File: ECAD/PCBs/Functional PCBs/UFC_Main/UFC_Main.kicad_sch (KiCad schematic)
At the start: 240 parts, among them J1 EXT_PWR, J2 ENC1, J3 VOL1, J4 BRT, J5 AP KB, J6 HUD BIT, J7 ENC2, J8 VOL2, J9 ADF SW, Q2 2N7002, Q4 ME2328-G, Q5 ME2328-G, Q6 ME2328-G, Q7 ME2328-G, Q8 ME2328-G, SW1 B3F-1026, U1 HT1621B, U10 TCA8418RTWR, U11 GN1640T, U12 GN1640T, U2 GN1640T, U3 GN1640T, U4 GN1640T, U5 GN1640T, U6 GN1640T, U7 GN1640T, U8 TXS0108EPWR, U9 TXS0108EPWR

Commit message: Updated scratchpad driver and power circuit
- Increased Board Rev to 6.2.0
- Change scratchpad driver vLCD resistor from 10k to 10ohm with a 10K trim pot in series.
  - **Justification:** Maximize the hardware-set brightness range.
- Power circuit changes:
  - **D39:** Change to [schottkey diode.](https://jlcpcb.com/partdetail/Goodwork-K24/C908664)
  - **Between Pin 2 of Q5 and VCC_SNS:** Add 10k pulldown to ground.
  - **Justification:** Did not function as intended.
    - [Link to new simulation](https://tinyurl.com/26gh26ra)

TBD:  **Q4, Q5, Q7, Q8:** Change to [p-channel MOSFETs from n-channel.](https://jlcpcb.com/partdetail/Shikues-SKML5203/C475707)
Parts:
- added R5: 10K, Resistor_SMD:R_0603_1608Metric, symbol Device:R_Small
- added RV2: 10K, Potentiometer_THT:Potentiometer_Bourns_3386P_Vertical, symbol Device:R_Potentiometer_Trim
- D39: value 1N4004W -> K24; symbol Diode:1N4004 -> Device:D_Schottky; LCSC C162732 -> C908664; Manufacturer PN 1N4001W -> K24; PN 1N4001W -> K24
- R2: value 10K -> 10; footprint Resistor_SMD:R_0603_1608Metric -> Capacitor_SMD:C_0402_1005Metric_Pad0.74x0.62mm_HandSolder; LCSC C25804 -> C25077; Manufacturer PN 0603WAF1002T5E -> 0402WGF100JTCE; PN 0603WAF1002T5E -> 0402WGF100JTCE
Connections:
- net +5V: now also RV2.1; no longer R2.1
- net GND: now also R5.2, RV2.3
- net VCC_SNS@3.3V: now also R5.1
- new net: R2.1, RV2.2
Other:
- moved on the sheet: R2

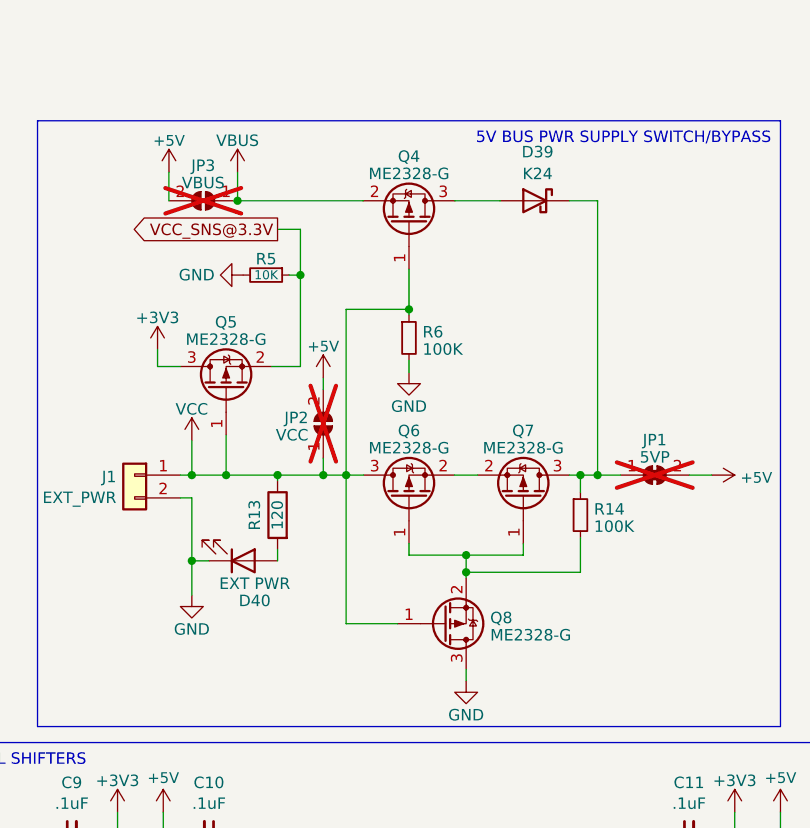
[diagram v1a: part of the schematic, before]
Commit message: Schematics (#1113)
- Q8
	changed Symbol to n-channel
      	switched drain and source
	Updated Datasheet and description
- Q4, Q6, Q7
	changed Part to SKML5203
	Updated Datasheet, description, LCSC and PN
PCB
- Q8
	Update routing according to schematic

Co-authored-by: scuba82 <christian_thalhammer@gmx.at>
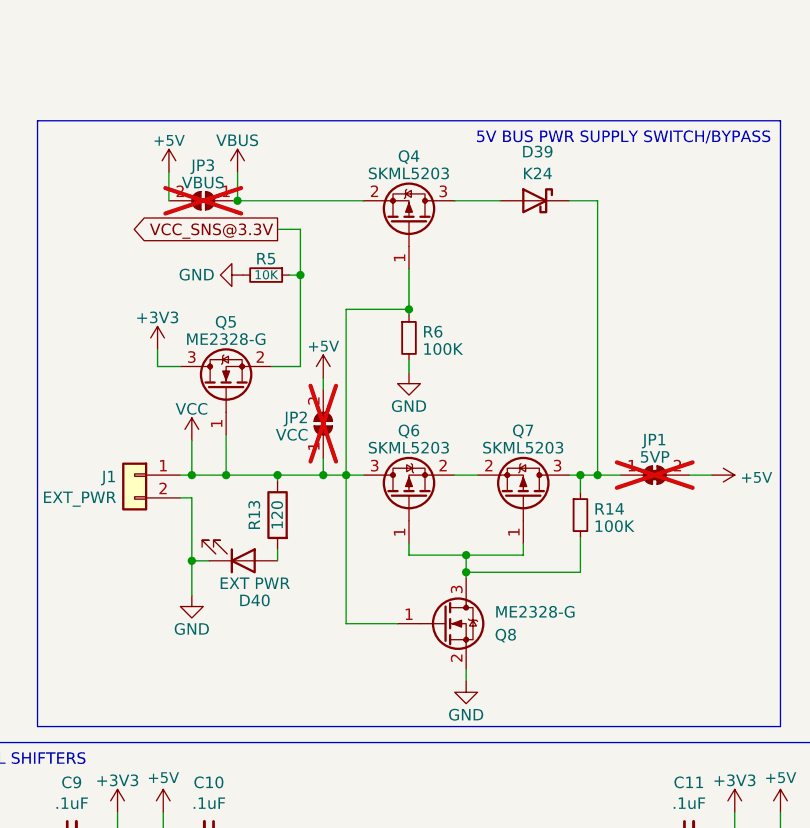
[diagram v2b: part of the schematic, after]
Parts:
- Q4, Q6, Q7: value ME2328-G -> SKML5203; LCSC C709746 -> C475707; PN ME2328-G -> SKML5203
- Q5, Q8: footprint Package_TO_SOT_SMD:SOT-23 -> Package_TO_SOT_SMD:SOT-323_SC-70; symbol Transistor_FET:BSS84 -> Transistor_FET:BSS214NW
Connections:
- net GND: now also Q8.2 (S); no longer Q8.3 (D)
- net at Q6.1 (G), Q7.1 (G), R14.2: now also Q8.3 (D); no longer Q8.2 (S)
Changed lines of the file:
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@@
 			)
 		)
-		(property "Value" "ME2328-G"
+		(property "Value" "SKML5203"
 			(at 709.295 62.4111 90)
 			(effects
@@
 			)
 		)
-		(property "Datasheet" "https://www.vishay.com/docs/68741/si2301cd.pdf"
+		(property "Datasheet" "https://www.lcsc.com/datasheet/lcsc_datasheet_2001131004_Shikues-SKML5203_C475707.pdf"
 			(at 709.295 67.945 0)
 			(effects
@@
 			)
 		)
-		(property "Description" ""
+		(property "Description" "30V 4A 65mΩ@10V,4A 1.3V@250uA 1 Piece P-Channel SOT-23 MOSFETs ROHS"
 			(at 709.295 67.945 0)
 			(effects
@@
 			)
 		)
-		(property "LCSC" "C709746"
+		(property "LCSC" "C475707"
 			(at 709.295 67.945 90)
 			(effects
@@
 			)
 		)
-		(property "PN" "ME2328-G"
+		(property "PN" "SKML5203"
 			(at 709.295 67.945 90)
 			(effects
@@
 			)
 		)
-		(property "Value" "ME2328-G"
+		(property "Value" "SKML5203"
 			(at 721.995 62.4111 90)
 			(effects
@@
 			)
 		)
-		(property "Datasheet" "https://www.vishay.com/docs/68741/si2301cd.pdf"
+		(property "Datasheet" "https://www.lcsc.com/datasheet/lcsc_datasheet_2001131004_Shikues-SKML5203_C475707.pdf"
 			(at 721.995 67.945 0)
 			(effects
@@
 			)
 		)
-		(property "Description" ""
+		(property "Description" "30V 4A 65mΩ@10V,4A 1.3V@250uA 1 Piece P-Channel SOT-23 MOSFETs ROHS"
 			(at 721.995 67.945 0)
 			(effects
@@
 			)
 		)
-		(property "LCSC" "C709746"
+		(property "LCSC" "C475707"
 			(at 721.995 67.945 90)
 			(effects
@@
 			)
 		)
-		(property "PN" "ME2328-G"
+		(property "PN" "SKML5203"
 			(at 721.995 67.945 90)
 			(effects
@@
 	)
 	(symbol
-		(lib_id "Transistor_FET:BSS84")
+		(lib_id "Transistor_FET:BSS214NW")
 		(at 713.105 81.915 0)
-		(mirror x)
 		(unit 1)
 		(exclude_from_sim no)
@@
 		(on_board yes)
 		(dnp no)
-		(fields_autoplaced yes)
 		(property "Reference" "Q8"
-			(at 718.312 81.2713 0)
+			(at 718.82 83.1851 0)
 			(effects
 				(font
@@
 		)
 		(property "Value" "ME2328-G"
-			(at 718.312 83.1923 0)
+			(at 718.82 80.6451 0)
 			(effects
 				(font
@@
 			)
 		)
-		(property "Footprint" "Package_TO_SOT_SMD:SOT-23"
-			(at 718.185 80.01 0)
+		(property "Footprint" "Package_TO_SOT_SMD:SOT-323_SC-70"
+			(at 718.185 83.82 0)
 			(effects
 				(font
@@
 			)
 		)
-		(property "Datasheet" "https://www.vishay.com/docs/68741/si2301cd.pdf"
-			(at 713.105 81.915 0)
+		(property "Datasheet" "https://www.lcsc.com/datasheet/lcsc_datasheet_2007241236_MATSUKI-ME2328-G_C709746.pdf"
+			(at 718.185 85.725 0)
 			(effects
 				(font
@@
 			)
 		)
-		(property "Description" ""
+		(property "Description" "105V 1.5A 230mΩ@10V,1.5A 1.3W 2V@250uA 1 N-Channel SOT-23 MOSFETs ROHS"
 			(at 713.105 81.915 0)
 			(effects
@@
 			)
 		)
-		(property "Value" "ME2328-G"
+		(property "Value" "SKML5203"
 			(at 709.295 31.9311 90)
 			(effects
@@
 			)
 		)
-		(property "Datasheet" "https://www.vishay.com/docs/68741/si2301cd.pdf"
+		(property "Datasheet" "https://www.lcsc.com/datasheet/lcsc_datasheet_2001131004_Shikues-SKML5203_C475707.pdf"
 			(at 709.295 37.465 0)
 			(effects
@@
 			)
 		)
-		(property "Description" ""
+		(property "Description" "30V 4A 65mΩ@10V,4A 1.3V@250uA 1 Piece P-Channel SOT-23 MOSFETs ROHS"
 			(at 709.295 37.465 0)
 			(effects
@@
 			)
 		)
-		(property "LCSC" "C709746"
+		(property "LCSC" "C475707"
 			(at 709.295 37.465 90)
 			(effects
@@
 			)
 		)
-		(property "PN" "ME2328-G"
+		(property "PN" "SKML5203"
 			(at 709.295 37.465 90)
 			(effects
@@
 	)
 	(symbol
-		(lib_id "Transistor_FET:BSS84")
+		(lib_id "Transistor_FET:BSS214NW")
 		(at 688.975 55.88 90)
 		(unit 1)
@@
 			)
 		)
-		(property "Footprint" "Package_TO_SOT_SMD:SOT-23"
+		(property "Footprint" "Package_TO_SOT_SMD:SOT-323_SC-70"
 			(at 690.88 50.8 0)
 			(effects
@@
 			)
 		)
-		(property "Datasheet" "https://www.vishay.com/docs/68741/si2301cd.pdf"
-			(at 688.975 55.88 0)
+		(property "Datasheet" "https://www.lcsc.com/datasheet/lcsc_datasheet_2007241236_MATSUKI-ME2328-G_C709746.pdf"
+			(at 692.785 50.8 0)
 			(effects
 				(font
@@
 			)
 		)
-		(property "Description" ""
+		(property "Description" "105V 1.5A 230mΩ@10V,1.5A 1.3W 2V@250uA 1 N-Channel SOT-23 MOSFETs ROHS"
 			(at 688.975 55.88 0)
 			(effects

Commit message: Added ADC for pots; changed BIT LED values
Added U13 & C18 (ADS115IDGS 4-CHANNEL ADC)
Rerouted pots to ADC from MC. (Cause ESP32 ADC sucks.)
Changed R43 & R44 from 68ohm to 120ohm to reduce brightness of BIT LEDs.
Generated fab package.
Updated files in release folder.
Was unable to reasonably move OPT 4/5 cues to new driver from COMM 2 driver. (Non-critical.)

Co-Authored-By: Oscar Arias <12484797+amanuense@users.noreply.github.com>
Co-Authored-By: Sandra Carroll <19305697+kbastronomics@users.noreply.github.com>
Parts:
- added C18: 10uF, Capacitor_SMD:C_0805_2012Metric, symbol Device:C_Small
- added U13: ADS1115IDGSR, Package_SO:VSSOP-10_3x3mm_P0.5mm, symbol Analog_ADC:ADS1115IDGS
- R43, R44: value 68 -> 120; LCSC C27592 -> C22787; Manufacturer PN 0603WAF680JT5E -> 0603WAF1200T5E; PN 0603WAF680JT5E -> 0603WAF1200T5E
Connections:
- net +3V3: now also C18.2, U13.8 (VDD)
- net GND: now also C18.1, U13.1 (ADDR), U13.3 (GND)
- net SCL@3.3V: now also U13.10 (SCL)
- net SDA@3.3V: now also U13.9 (SDA)
- net ANALOG1@3.3V renamed AIN1
- net AIN1: now also U13.5 (AIN1); no longer MC1.9 (IO1)
- net ANALOG2@3.3V renamed AIN0
- net AIN0: now also U13.4 (AIN0); no longer MC1.10 (IO2)
- net ANALOG3@3.3V renamed AIN2
- net AIN2: now also U13.6 (AIN2); no longer MC1.2 (IO3)
- new net ADC_RDY@3.3V: MC1.9 (IO1), U13.2 (ALERT/RDY)
- no-connect marks 123 -> 126
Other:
- note added: "ADDR GND: 1001000 VDD: 1001001 SDA: 1001010 SCL: 1001011"
- moved on the sheet: C5, C6, C7, C8, D69, D70, D71, D72, D73, D74, D75, D76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

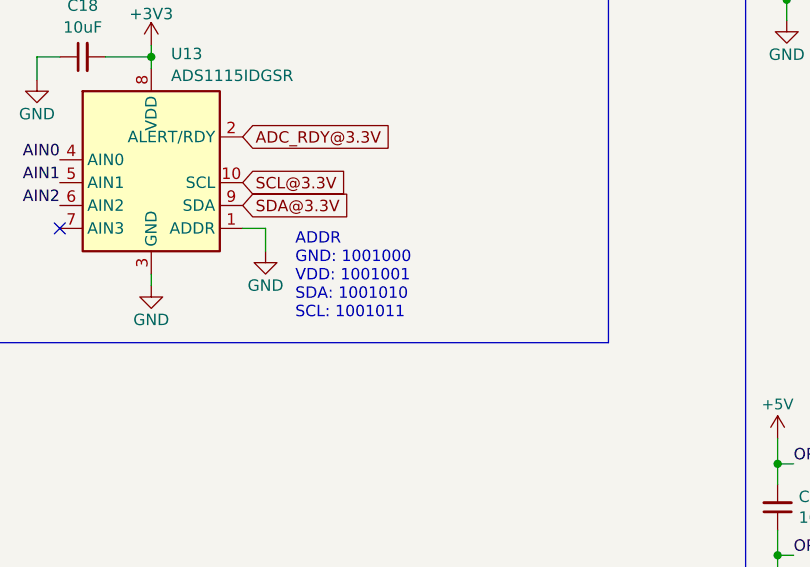
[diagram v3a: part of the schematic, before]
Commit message: Update UFC_Main.kicad_sch
Added Hex codes to ADC address note.
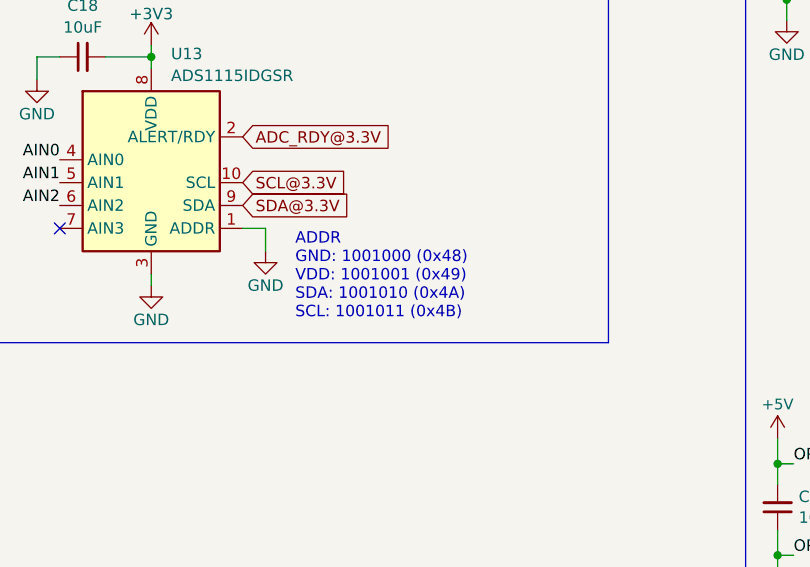
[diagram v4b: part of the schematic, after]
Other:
- note added: "ADDR GND: 1001000 (0x48) VDD: 1001001 (0x49) SDA: 1001010 (0x4A) SCL: 1001011 (0x4B)"
- note removed: "ADDR GND: 1001000 VDD: 1001001 SDA: 1001010 SCL: 1001011"
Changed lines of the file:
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@@
 		)
 	)
-	(text "ADDR\nGND: 1001000\nVDD: 1001001\nSDA: 1001010\nSCL: 1001011"
+	(text "ADDR\nGND: 1001000 (0x48)\nVDD: 1001001 (0x49)\nSDA: 1001010 (0x4A)\nSCL: 1001011 (0x4B)"
 		(exclude_from_sim no)
 		(at 231.902 278.384 0)

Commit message: Added 3x solder pads
Added Solder Pads for 2x unused GPIO and unused ADC channel.
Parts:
- added J10: GPIO3, Connector_Wire:SolderWirePad_1x01_SMD_1x2mm, symbol Connector:Conn_01x01_Pin
- added J11: GPIO2, Connector_Wire:SolderWirePad_1x01_SMD_1x2mm, symbol Connector:Conn_01x01_Pin
- added J12: AIN3, Connector_Wire:SolderWirePad_1x01_SMD_1x2mm, symbol Connector:Conn_01x01_Pin
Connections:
- net at MC1.10 (IO2): now also J11.1 (Pin_1)
- net at MC1.2 (IO3): now also J10.1 (Pin_1)
- net at U13.7 (AIN3): now also J12.1 (Pin_1)
- no-connect marks 126 -> 123
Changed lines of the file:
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@@
 	)
 	(no_connect
-		(at 803.91 46.99)
-	)
-	(no_connect
 		(at 317.5 201.93)
 	)
@@
 	)
 	(no_connect
-		(at 205.74 273.05)
-	)
-	(no_connect
 		(at 340.36 410.21)
 	)
@@
 	)
 	(no_connect
-		(at 803.91 24.13)
-	)
-	(no_connect
 		(at 340.36 382.27)
 	)
@@
 	(wire
 		(pts
+			(xy 203.2 273.05) (xy 205.74 273.05)
+		)
+		(stroke
+			(width 0)
+			(type default)
+		)
+	)
+	(wire
+		(pts
 			(xy 341.63 312.42) (xy 339.09 312.42)
 		)
@@
 	(wire
 		(pts
+			(xy 788.67 46.99) (xy 803.91 46.99)
+		)
+		(stroke
+			(width 0)
+			(type default)
+		)
+	)
+	(wire
+		(pts
 			(xy 308.61 127) (xy 317.5 127)
 		)
@@
 	(wire
 		(pts
+			(xy 801.37 24.13) (xy 803.91 24.13)
+		)
+		(stroke
+			(width 0)
+			(type default)
+		)
+	)
+	(wire
+		(pts
 			(xy 555.625 306.07) (xy 574.675 306.07)
 		)
@@
 	)
 	(symbol
+		(lib_id "Connector:Conn_01x01_Pin")
+		(at 198.12 273.05 0)
+		(unit 1)
+		(exclude_from_sim no)
+		(in_bom yes)
+		(on_board yes)
+		(dnp no)
+		(fields_autoplaced yes)
+		(property "Reference" "J12"
+			(at 198.755 268.8293 0)
+			(effects
+				(font
+					(size 1.27 1.27)
+				)
+			)
+		)
+		(property "Value" "AIN3"
+			(at 198.755 271.2536 0)
+			(effects
+				(font
+					(size 1.27 1.27)
+				)
+			)
+		)
+		(property "Footprint" "Connector_Wire:SolderWirePad_1x01_SMD_1x2mm"
+			(at 198.12 273.05 0)
+			(effects
+				(font
+					(size 1.27 1.27)
+				)
+				(hide yes)
+			)
+		)
+		(property "Datasheet" "~"
+			(at 198.12 273.05 0)
+			(effects
+				(font
+					(size 1.27 1.27)
+				)
+				(hide yes)
+			)
+		)
+		(property "Description" "Generic connector, single row, 01x01, script generated"
+			(at 198.12 273.05 0)
+			(effects
+				(font
+					(size 1.27 1.27)
+				)
+				(hide yes)
+			)
+		)
+		(pin "1"
+		)
+		(instances
+			(project ""
+				(path "/a592f7ca-173a-431b-8b1a-54c8908b4230"
+					(reference "J12")
+					(unit 1)
+				)
+			)
+		)
+	)
+	(symbol
 		(lib_name "GND_1")
 		(lib_id "power:GND")
@@
 	)
 	(symbol
+		(lib_id "Connector:Conn_01x01_Pin")
+		(at 796.29 24.13 0)
+		(unit 1)
+		(exclude_from_sim no)
+		(in_bom yes)
+		(on_board yes)
+		(dnp no)
+		(property "Reference" "J10"
+			(at 796.925 19.9093 0)
+			(effects
+				(font
+					(size 1.27 1.27)
+				)
+			)
+		)
+		(property "Value" "GPIO3"
+			(at 795.528 22.352 0)
+			(effects
+				(font
+					(size 1.27 1.27)
+				)
+			)
+		)
+		(property "Footprint" "Connector_Wire:SolderWirePad_1x01_SMD_1x2mm"
+			(at 796.29 24.13 0)
+			(effects
+				(font
+					(size 1.27 1.27)
+				)
+				(hide yes)
+			)
+		)
+		(property "Datasheet" "~"
+			(at 796.29 24.13 0)
+			(effects
+				(font
+					(size 1.27 1.27)
+				)
+				(hide yes)
+			)
+		)
+		(property "Description" "Generic connector, single row, 01x01, script generated"
+			(at 796.29 24.13 0)
+			(effects
+				(font
+					(size 1.27 1.27)
+				)
+				(hide yes)
+			)
+		)
+		(pin "1"
+		)
+		(instances
+			(project "UFC_Main"
+				(path "/a592f7ca-173a-431b-8b1a-54c8908b4230"
+					(reference "J10")
+					(unit 1)
+				)
+			)
+		)
+	)
+	(symbol
 		(lib_id "KiCadCustomLib:Omron_B3F-1026")
 		(at 208.915 208.28 0)
@@
 					(unit 1)
 				)
+			)
+		)
+	)
+	(symbol
+		(lib_id "Connector:Conn_01x01_Pin")
+		(at 783.59 46.99 0)
+		(unit 1)
+		(exclude_from_sim no)
+		(in_bom yes)
+		(on_board yes)
+		(dnp no)
+		(property "Reference" "J11"
+			(at 784.225 42.7693 0)
+			(effects
+				(font
+					(size 1.27 1.27)
+				)
+			)
+		)
+		(property "Value" "GPIO2"
+			(at 782.828 45.212 0)
+			(effects
+				(font
+					(size 1.27 1.27)
+				)
+			)
+		)
+		(property "Footprint" "Connector_Wire:SolderWirePad_1x01_SMD_1x2mm"
+			(at 783.59 46.99 0)
+			(effects
+				(font
+					(size 1.27 1.27)
+				)
+				(hide yes)
+			)
+		)
+		(property "Datasheet" "~"
+			(at 783.59 46.99 0)
+			(effects
+				(font
+					(size 1.27 1.27)
+				)
+				(hide yes)
+			)
+		)
+		(property "Description" "Generic connector, single row, 01x01, script generated"
+			(at 783.59 46.99 0)
+			(effects
+				(font
+					(size 1.27 1.27)
+				)
+				(hide yes)
+			)
+		)
+		(pin "1"
+		)
+		(instances
+			(project "UFC_Main"
+				(path "/a592f7ca-173a-431b-8b1a-54c8908b4230"
+					(reference "J11")
+					(unit 1)
+				)

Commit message: Updated UFC ADC/Pot circuit & replaced obsolete parts (#1171)
* Add +2V5 reference and I2C header to UFC_Main PCB

Introduced a +2V5 voltage reference circuit using ADR5040ARTZ and supporting components. Added a new 5V I2C pin header (J13). Updated net assignments and component placements to support the new reference and header. Minor changes to silkscreen and attributes for several footprints.

Co-Authored-By: Sandra Carroll <19305697+kbastronomics@users.noreply.github.com>

* Add test points for 3V3 and 2V5 rails

Added TP20 (3V3) and TP21 (2V5) test points to the UFC_Main PCB and updated corresponding net segments. Also fixed minor silkscreen and code formatting issues in the PCB layout and schematic files. Removed auto-saved files from the project directory.

Co-Authored-By: Sandra Carroll <19305697+kbastronomics@users.noreply.github.com>

* Replaced obsolete parts and generated gerbers

Replaced obsolete 100k 0402 resistors and N-Channel MOSFETS in power circuit.
Generated JLCPCB manufacturing package.
Generated 3D STEP file.

Co-Authored-By: Sandra Carroll <19305697+kbastronomics@users.noreply.github.com>

* Update UFC_Main PCB BOM, CPL, and schematic

Schematic notes updated to specify display package, and CPL/GERBER/PDF files regenerated to reflect these changes and copied to release folder.

* Update UFC_Main PCB production files

Regenerated manufacturing files due to a BOM/CPL mismatch.

---------

Co-authored-by: Sandra Carroll <19305697+kbastronomics@users.noreply.github.com>
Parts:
- added C19: .1uF, Capacitor_SMD:C_0603_1608Metric, symbol Device:C_Small
- added J13: 5V I2C, Connector_PinHeader_2.54mm:PinHeader_1x04_P2.54mm_Vertical, symbol Connector_Generic:Conn_01x04
- added R15: 120, Resistor_SMD:R_0603_1608Metric, symbol Device:R_Small
- added TP20: 3V3, TestPoint:TestPoint_THTPad_D1.5mm_Drill0.7mm, symbol Connector:TestPoint_Alt
- added TP21: 2V5, TestPoint:TestPoint_THTPad_D1.5mm_Drill0.7mm, symbol Connector:TestPoint_Alt
- added U14: ADR5040ARTZ, Package_TO_SOT_SMD:SOT-23-3, symbol KiCadCustomLib:ADR5040ARTZ
- C18: footprint Capacitor_SMD:C_0805_2012Metric -> Capacitor_SMD:C_0402_1005Metric; LCSC C15850 -> C15525; PN CL21A106KAYNNNE -> CL05A106MQ5NUNC
- Q5, Q8: value ME2328-G -> SI2302; footprint Package_TO_SOT_SMD:SOT-323_SC-70 -> OH_Footprints:SOT-23; LCSC C709746 -> C2891732; Manufacturer PN ME2328-G -> SI2302; PN ME2328-G -> SI2302
- R14, R6: LCSC C327804 -> C25741; Manufacturer PN MR04X104 JTL -> 0402WGF1003TCE; PN MR04X104 JTL -> 0402WGF1003TCE
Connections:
- net +3V3: now also C19.2, R15.1, TP20.1; no longer C5.2, C6.2, C8.2, J3.1 (Pin_1), J4.1 (Pin_1), J8.1 (Pin_1)
- net +5V: now also J13.2 (Pin_2)
- net AIN0: now also C6.2; no longer C6.1
- net AIN1: now also C5.2; no longer C5.1
- net AIN2: now also C8.2; no longer C8.1
- net GND: now also C5.1, C6.1, C8.1, C19.1, J13.1 (Pin_1), U14.2 (V-)
- net SCL: now also J13.4 (Pin_4)
- net SDA: now also J13.3 (Pin_3)
- new net +2V5: J3.1 (Pin_1), J4.1 (Pin_1), J8.1 (Pin_1), R15.2, TP21.1, U14.1 (V+), U14.3 (T)
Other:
- moved on the sheet: C18, C5, C6, C8, J12, J3, J4, J8, U13
